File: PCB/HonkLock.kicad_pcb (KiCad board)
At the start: 2 copper layers, 55.9 x 30.5 mm, 9 parts, among them J1 Conn_01x03_Pin, J2 Conn_01x06_Pin, J3 Conn_01x04_Pin, U1 Waveshare_ESP32_S3_Zero

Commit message: Carrier board PCB
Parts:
- added SW1: SW_Push, Button_Switch_THT:SW_PUSH_6mm, F.Cu at (221.9, 66.2)
- added SW2: SW_Push, Button_Switch_THT:SW_PUSH_6mm, F.Cu at (212.2, 66.2)
- added SW3: SW_Push, Button_Switch_THT:SW_PUSH_6mm, F.Cu at (202.5, 66.2)
- moved H1 8.98 mm to (191.3, 63.2)
- moved H3 8.67 mm to (227.5, 63.2)
- moved G*** 7.88 mm to (206.5, 80.3)
- moved J2 7.74 mm to (226.7, 74.5)
- moved H2 6.60 mm to (191.3, 92.7)
- moved H4 6.02 mm to (227.7, 92.7)
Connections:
- U1 pad 5: unconnected-(U1-GP2-Pad5) -> Net-(U1-GP2)
- U1 pad 6: unconnected-(U1-GP3-Pad6) -> Net-(U1-GP3)
- U1 pad 7: unconnected-(U1-GP4-Pad7) -> Net-(U1-GP4)
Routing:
- net Net-(U1-GP2): track 0.00 -> 26.2 mm
- net Net-(U1-GP3): track 0.00 -> 19.5 mm
- net Net-(U1-GP4): track 0.00 -> 12.7 mm
- net VDD: track 41.5 -> 35.1 mm
- net unconnected-(U1-GP6-Pad9): track 0.00 -> 0.57 mm
- net unconnected-(U1-GP5-Pad8): track 0.00 -> 0.57 mm
- net GND: vias 2 -> 5
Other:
- board size 55.9 x 30.5 mm -> 43 x 36.2 mm
- board text added: "A L G 3v"
- board text added: "Motor"
- board text added: "S 5V G"
- board text added: "Sensor"

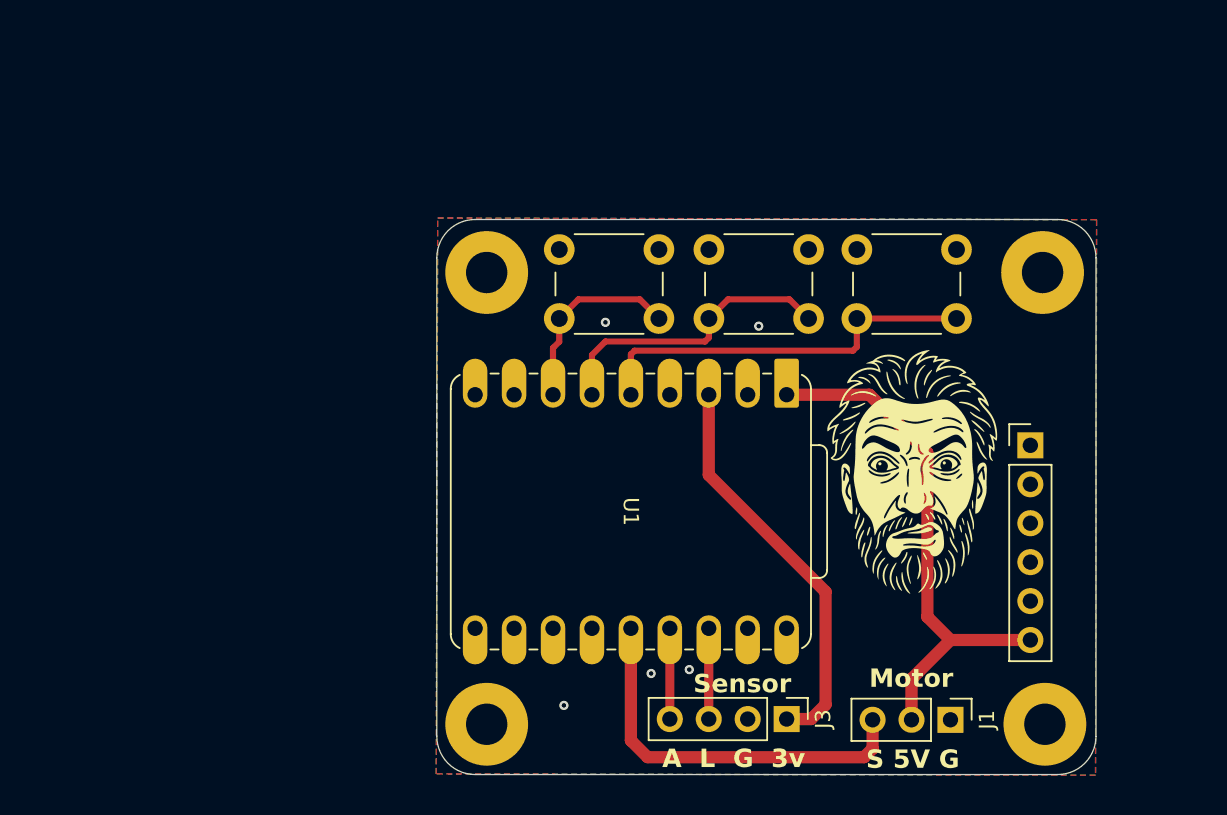
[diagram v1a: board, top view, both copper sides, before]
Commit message: switched to the correct ESP32 dev board, added a capacitor, added a forth switch
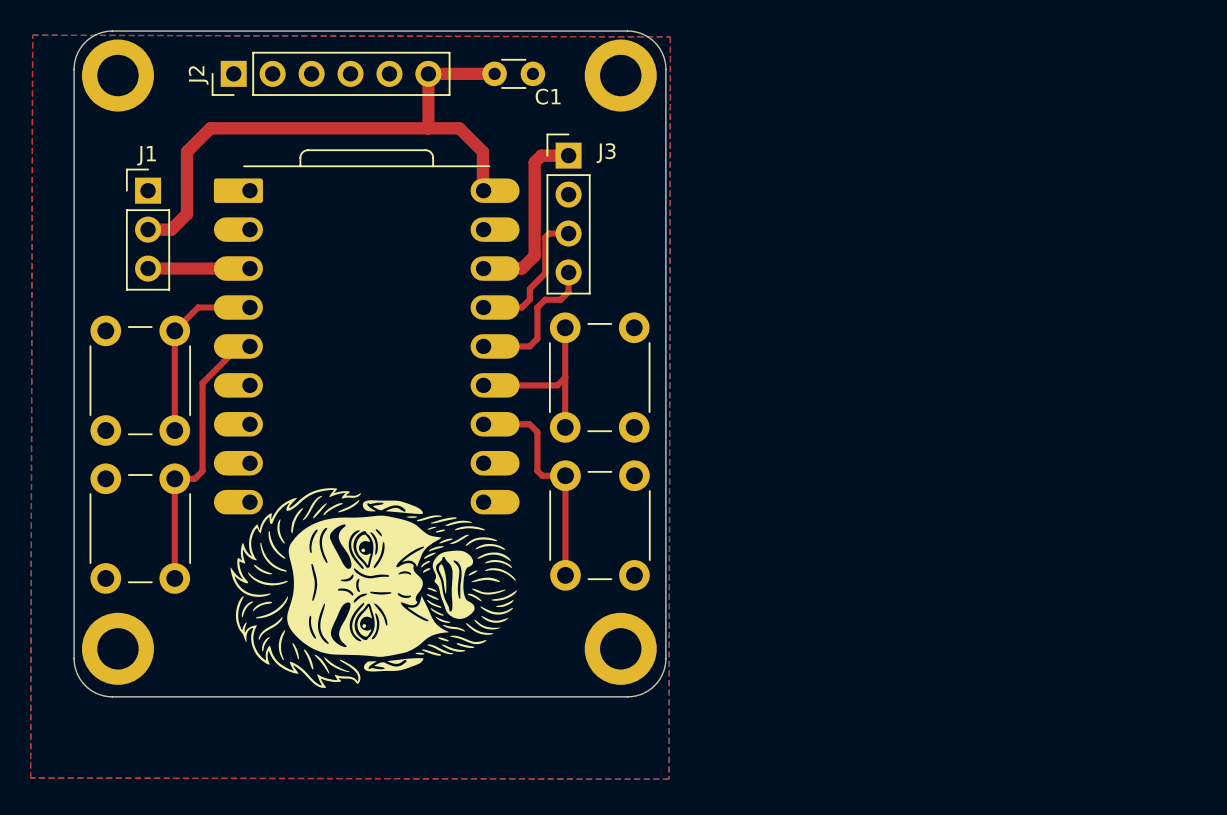
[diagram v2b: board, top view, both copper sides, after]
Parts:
- removed H1, H2, H3, H4: MountingHole, MountingHole:MountingHole_2.7mm_M2.5_Pad
- removed U1: Waveshare_ESP32_S3_Zero, Paul:Waveshare_ESP32_S3_Zero_Unspecified
- added C1: 0.1uF, Capacitor_THT:C_Disc_D3.0mm_W1.6mm_P2.50mm, F.Cu at (194.3, 50.3)
- added REF**: MountingHole_2.7mm_M2.5_DIN965_Pad, MountingHole:MountingHole_2.7mm_M2.5_DIN965_Pad, F.Cu at (200.0, 50.4)
- added REF**: MountingHole_2.7mm_M2.5_DIN965_Pad, MountingHole:MountingHole_2.7mm_M2.5_DIN965_Pad, F.Cu at (167.2, 50.4)
- added REF**: MountingHole_2.7mm_M2.5_DIN965_Pad, MountingHole:MountingHole_2.7mm_M2.5_DIN965_Pad, F.Cu at (200.0, 87.8)
- added REF**: MountingHole_2.7mm_M2.5_DIN965_Pad, MountingHole:MountingHole_2.7mm_M2.5_DIN965_Pad, F.Cu at (167.2, 87.8)
- added SW4: SW_Push, Button_Switch_THT:SW_PUSH_6mm, F.Cu at (196.4, 83.0)
- added U2: ESP32-S3-SUPERMINI, Circuits:ESP32_S3_Supermini, F.Cu at (183.4, 65.5)
- moved J1 62.7 mm to (169.2, 57.9), turned to 0 degrees
- moved J2 57.3 mm to (174.8, 50.3), turned to 90 degrees
- moved SW2 42.6 mm to (170.9, 76.7), turned to -90 degrees
- moved J3 39.4 mm to (196.6, 55.6), turned to 0 degrees
- moved SW3 31.6 mm to (170.9, 67.1), turned to -90 degrees
- moved SW1 26.5 mm to (196.4, 73.4), turned to 90 degrees
- moved G*** 26.0 mm to (182.2, 71.0), turned to 90 degrees
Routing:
- net Net-(J1-Pin_3): track 25.7 -> 6.65 mm
- net Net-(SW4-Pad1): track 0.00 -> 14.7 mm
- net Net-(SW1-Pad1): track 26.2 -> 12.0 mm
- net 3v3: track 26.3 -> 12.2 mm
- net Net-(J3-Pin_4): track 5.92 -> 11.5 mm
- net Net-(J3-Pin_3): track 5.92 -> 9.33 mm
- net VDD: track 35.1 -> 38.0 mm
- net Net-(SW2-Pad1): track 19.5 -> 18.3 mm
- net Net-(SW3-Pad1): track 12.7 -> 12.0 mm
- net unconnected-(U1-GP6-Pad9): track 0.57 -> 0.00 mm
- net unconnected-(U1-GP5-Pad8): track 0.57 -> 0.00 mm
- net GND: vias 5 -> 0
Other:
- board size 43 x 36.2 mm -> 38.6 x 43.4 mm
- board text removed: "A L G 3v"
- board text removed: "Motor"
- board text removed: "S 5V G"
- board text removed: "Sensor"

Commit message: minor rev
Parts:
- added kibuzzard-6A52EB91: G***, kibuzzard-6A52EB91, B.Cu at (188.2, 83.4)
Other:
- board text added: "3v3"
- board text added: "5V"
- board text added: "5v"
- board text added: "DIN"
- board text added: "GND"
- board text added: "GND 5V"
- board text added: "Motor"
- board text added: "SCL"
- board text added: "SDA"
- board text added: "Sensor"
